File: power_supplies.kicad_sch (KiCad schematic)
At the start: 41 parts, among them IC1 ECP5-BGA256, U15 1V8REG, U3 3V3REG, U4 1V15REG, U5 2V5REG

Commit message: rename libraries from luna to cynthion
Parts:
- IC1: footprint luna:lattice_cabga256 -> cynthion:lattice_cabga256
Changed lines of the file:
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@@
     (property "Reference" "IC1" (id 0) (at 231.14 82.0928 0))
     (property "Value" "ECP5-BGA256" (id 1) (at 231.14 84.4042 0))
-    (property "Footprint" "luna:lattice_cabga256" (id 2) (at 130.81 -1.27 0)
+    (property "Footprint" "cynthion:lattice_cabga256" (id 2) (at 130.81 -1.27 0)
       (effects (font (size 1.27 1.27)) (justify left) hide)
     )

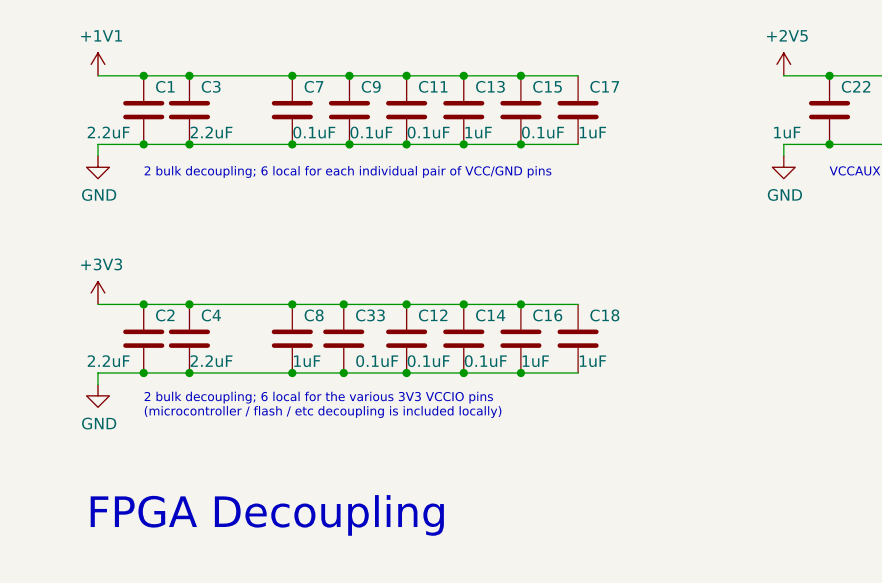
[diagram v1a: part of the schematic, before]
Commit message: Improve FPGA decoupling capacitor placement
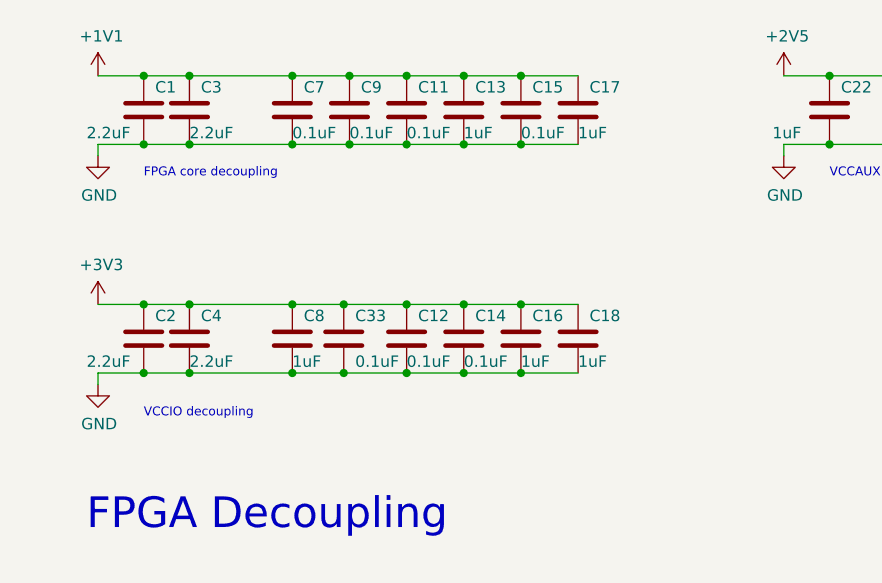
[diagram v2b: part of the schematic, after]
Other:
- note added: "FPGA core decoupling"
- note added: "VCCIO decoupling"
- note removed: "2 bulk decoupling; 6 local for each individual pair of VCC/GND pins"
- note removed: "2 bulk decoupling; 6 local for the various 3V3 VCCIO pins (microcontroller / flash / etc decoupling is included locally)"
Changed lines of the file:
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@@
     (stroke (width 0) (type default) (color 0 0 0 0))
   )
-  (text "2 bulk decoupling; 6 local for the various 3V3 VCCIO pins\n(microcontroller / flash / etc decoupling is included locally)"
-    (at 26.67 59.69 0)
+  (text "VCCIO decoupling" (at 26.67 59.69 0)
     (effects (font (size 0.9906 0.9906)) (justify left bottom))
   )
@@
     (effects (font (size 3.4036 3.4036)) (justify left bottom))
   )
-  (text "2 bulk decoupling; 6 local for each individual pair of VCC/GND pins"
-    (at 26.67 33.02 0)
+  (text "FPGA core decoupling" (at 26.67 33.02 0)
     (effects (font (size 0.9906 0.9906)) (justify left bottom))
   )

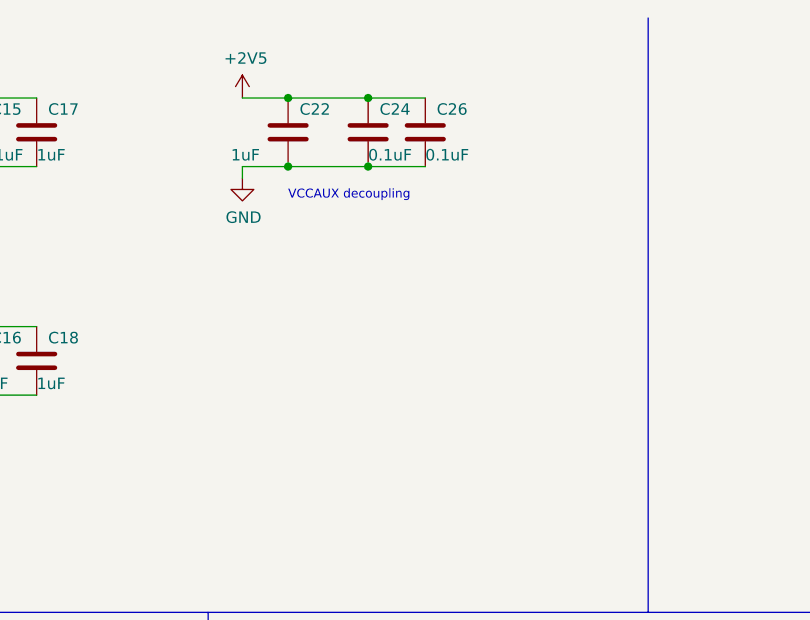
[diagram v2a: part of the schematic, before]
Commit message: Add pseudo-VCCIO and pseudo-GND pins, decoupling
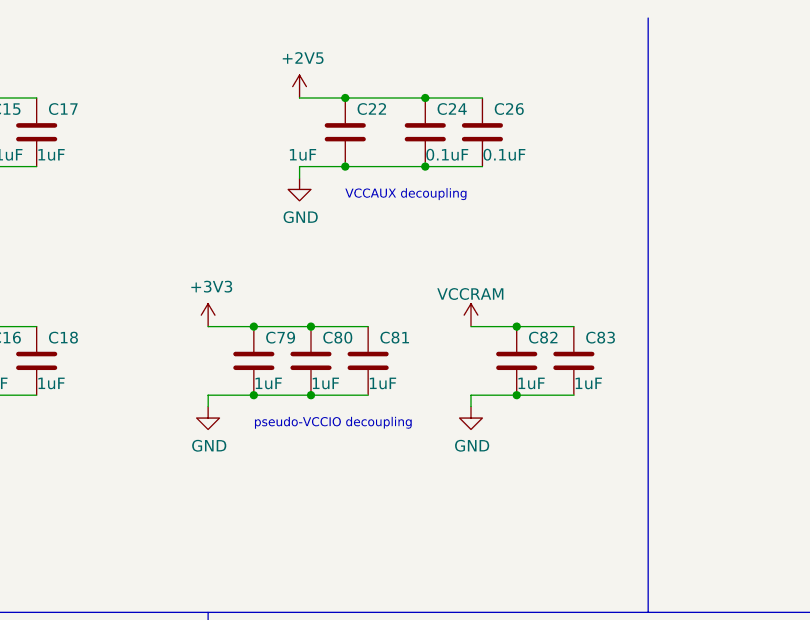
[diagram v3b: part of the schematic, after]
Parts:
- added C79, C80, C81, C82, C83: 1uF, Capacitor_SMD:C_0402_1005Metric, symbol Device:C
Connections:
- net +3V3: now also C79.1, C80.1, C81.1
- net GND: now also C79.2, C80.2, C81.2, C82.2, C83.2
- net VCCRAM: now also C82.1, C83.1
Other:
- note added: "pseudo-VCCIO decoupling"
- moved on the sheet: C22, C24, C26
